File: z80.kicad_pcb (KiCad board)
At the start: 2 copper layers, 104.8 x 111.8 mm, 37 parts, among them P2 CONN_01X02, P3 Jumper, SW1 RESET, U1 Z80CPU, U2 DIP_OSCILLATOR, U3 ATF16V8CV

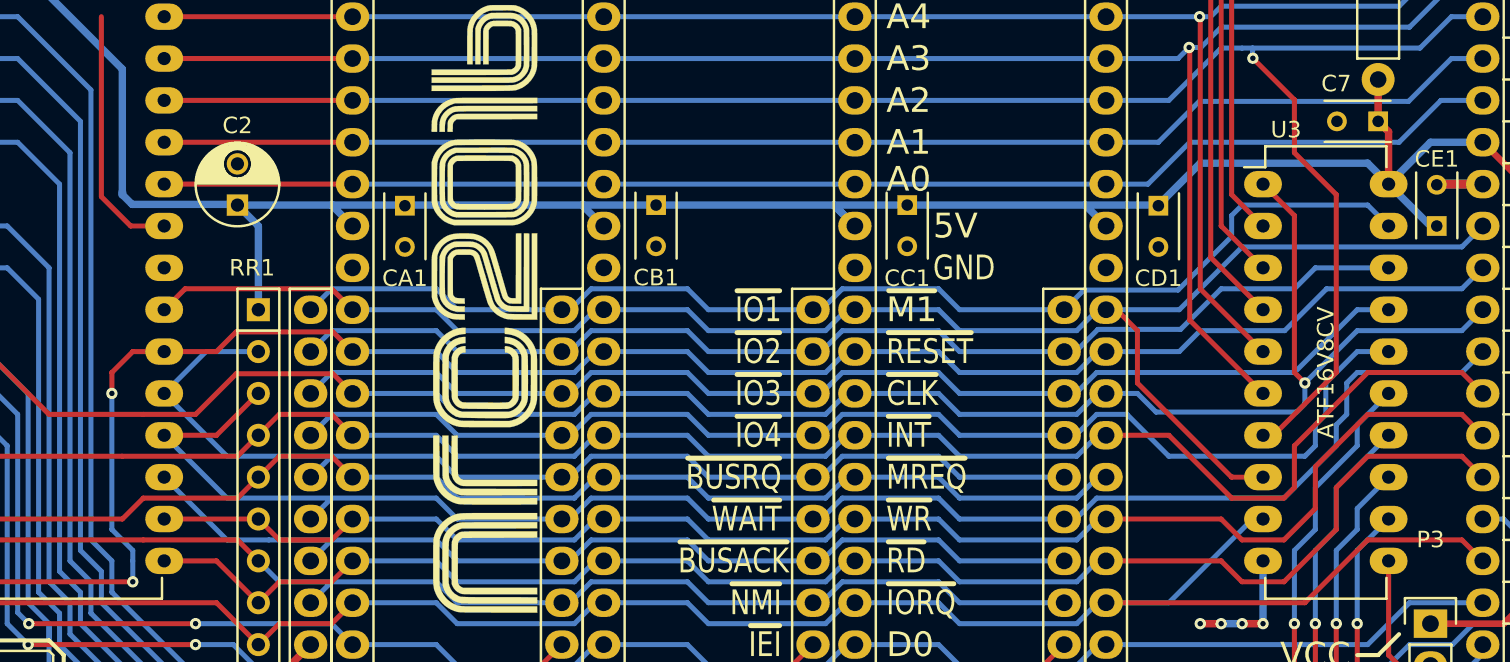
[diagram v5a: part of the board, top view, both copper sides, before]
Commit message: Fix screw up with VCC and GND on rc2014 slots.
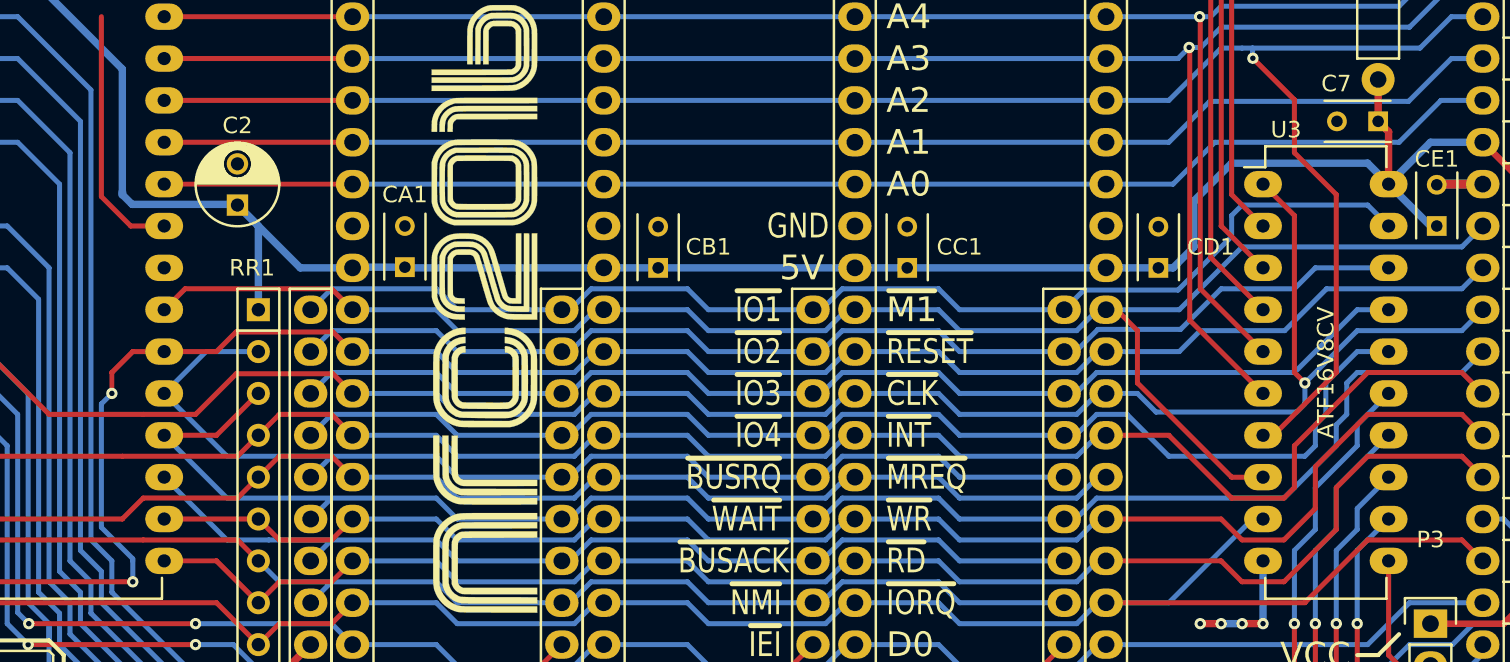
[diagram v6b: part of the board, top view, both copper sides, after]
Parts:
- moved LOGO2 5.23 mm to (95.8, 77.5)
- moved CB1 3.81 mm to (92.2, 81.3), turned to 90 degrees
- moved CC1 3.81 mm to (107.3, 81.3), turned to 90 degrees
- moved CD1 3.77 mm to (122.6, 81.3), turned to 90 degrees
- moved CA1 3.73 mm to (76.8, 81.2), turned to 90 degrees
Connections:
- net /CPU/A0 renamed /A0
- net /CPU/A1 renamed /A1
- net /CPU/A10 renamed /A10
- net /CPU/A11 renamed /A11
- net /CPU/A12 renamed /A12
- net /CPU/A13 renamed /A13
- net /CPU/A14 renamed /A14
- net /CPU/A15 renamed /A15
- net /CPU/A2 renamed /A2
- net /CPU/A3 renamed /A3
- net /CPU/A4 renamed /A4
- net /CPU/A5 renamed /A5
- net /CPU/A6 renamed /A6
- net /CPU/A7 renamed /A7
- net /CPU/A8 renamed /A8
- net /CPU/A9 renamed /A9
- net /CPU/D0 renamed /D0
- net /CPU/D1 renamed /D1
- net /CPU/D2 renamed /D2
- net /CPU/D3 renamed /D3
- net /CPU/D4 renamed /D4
- net /CPU/D5 renamed /D5
- net /CPU/D6 renamed /D6
- net /CPU/D7 renamed /D7
- net /CPU/~BUSACK renamed /~BUSACK
- net /CPU/~BUSRQ renamed /~BUSRQ
- net /CPU/~CLK renamed /~CLK
- net /CPU/~INT renamed /~INT
- net /CPU/~IORQ renamed /~IORQ
- net /CPU/~M1 renamed /~M1
- net /CPU/~MREQ renamed /~MREQ
- net /CPU/~NMI renamed /~NMI
- net /CPU/~RD renamed /~RD
- net /CPU/~RESET renamed /~RESET
- net /CPU/~WAIT renamed /~WAIT
- net /CPU/~WR renamed /~WR
- net /Card Slots/Expansion/RX renamed /Card Slots/RX
- net /Card Slots/Expansion/SPARE1 renamed /Card Slots/S1
- net /Card Slots/Expansion/SPARE2 renamed /Card Slots/S2
- net /Card Slots/Expansion/SPARE3 renamed /Card Slots/S3
- net /Card Slots/Expansion/TX renamed /Card Slots/TX
- net /Card Slots/PortA/SPARE4 renamed /Card Slots/S4
- net /Card Slots/PortA/~IOSEL0 renamed /Card Slots/~IOSEL0
- net /Card Slots/PortA/~IOSEL1 renamed /Card Slots/~IOSEL1
- net /Card Slots/PortA/~IOSEL2 renamed /Card Slots/~IOSEL2
- net /Card Slots/PortA/~IOSEL3 renamed /Card Slots/~IOSEL3
- PA1 pad 17: VCC -> GND
- PA1 pad 18: GND -> VCC
- PB1 pad 17: VCC -> GND
- PB1 pad 18: GND -> VCC
- PC1 pad 17: VCC -> GND
- PC1 pad 18: GND -> VCC
- PD1 pad 17: VCC -> GND
- PD1 pad 18: GND -> VCC
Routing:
- net VCC: track 310.8 -> 306.6 mm
- net /~RESET: track 168.6 -> 169.1 mm
